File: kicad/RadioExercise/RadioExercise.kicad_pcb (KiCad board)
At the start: 2 copper layers, 22 parts, among them IC1 HT82V739, IC2 PIC16F1778-I_SP, IC3 SST26VF064B-104I_SM, J1 Conn_01x02_Female, SW1 SW_MEC_5E, SW2 SW_MEC_5E, SW3 SW_MEC_5E, SW4 SW_MEC_5E, SW5 SW_DPDT_x2

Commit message: update
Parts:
- removed D1: LED, LED_THT:LED_D5.0mm_Clear
- removed R1: 10k, Resistor_THT:R_Axial_DIN0207_L6.3mm_D2.5mm_P7.62mm_Horizontal
- removed R6: 1k, Resistor_THT:R_Axial_DIN0207_L6.3mm_D2.5mm_P7.62mm_Horizontal
- removed SW3, SW4: SW_MEC_5E, Button_Switch_THT:SW_PUSH_6mm
- SW1, SW2: value SW_MEC_5E -> SW_Push
- moved SW5 58.7 mm to (171.1, 83.6)
- moved SW1 45.2 mm to (169.4, 75.9)
- moved R3 44.1 mm to (180.0, 63.8)
- moved R5 44.1 mm to (180.0, 67.8)
- moved C3 43.2 mm to (185.9, 72.6)
- moved C1 36.0 mm to (191.2, 65.0)
- moved J1 33.9 mm to (172.9, 71.8)
- moved LS1 33.8 mm to (162.1, 75.8)
- moved IC1 32.7 mm to (158.4, 63.8)
- moved IC2 32.7 mm to (151.2, 80.3)
- moved C5 24.2 mm to (180.0, 78.2)
- moved R2 22.3 mm to (169.2, 63.8)
- moved R4 22.3 mm to (169.2, 67.8)
- moved C4 13.7 mm to (158.8, 96.5)
- moved IC3 13.5 mm to (162.0, 89.8)
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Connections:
- IC2 pad 11: Net-(IC2-Pad11) -> GND
- SW1 pad 2: Net-(SW1-Pad2) -> Net-(IC2-Pad12)
- SW2 pad 2: Net-(SW2-Pad2) -> Net-(IC2-Pad13)

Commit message: update1
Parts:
- moved R2 62.1 mm to (147.3, 121.9), turned to 90 degrees
- moved C1 59.6 mm to (147.3, 105.4), turned to 270 degrees
- moved R3 48.2 mm to (184.2, 111.8), turned to 90 degrees
- moved SW2 47.3 mm to (180.3, 121.9), turned to 180 degrees
- moved C2 46.0 mm to (156.2, 111.8), turned to 180 degrees
- moved SW1 44.4 mm to (152.4, 116.8)
- moved C3 40.6 mm to (175.3, 111.8)
- moved SW5 39.5 mm to (188.0, 119.4), turned to 90 degrees
- moved R5 35.7 mm to (151.1, 88.9)
- moved R4 33.1 mm to (147.3, 92.7), turned to 270 degrees
- moved IC1 29.8 mm to (151.1, 92.7)
- moved IC2 29.4 mm to (166.4, 105.4)
- moved J1 27.2 mm to (186.7, 95.2), turned to 270 degrees
- moved LS1 26.0 mm to (143.5, 94.0), turned to 270 degrees
- moved IC3 18.0 mm to (176.5, 100.3), turned to 90 degrees
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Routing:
- net VDD: track 0.00 -> 110.4 mm
- net Net-(J1-Pad2): track 0.00 -> 18.3 mm

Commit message: remove wire
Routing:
- net VDD: track 110.4 -> 0.00 mm
- net Net-(J1-Pad2): track 18.3 -> 0.00 mm

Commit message: wire
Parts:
- J1, LS1: moved to B.Cu
- moved C3 47.8 mm to (207.0, 76.0), turned to 270 degrees
- moved J1 46.7 mm to (215.9, 58.8), turned to 90 degrees
- moved LS1 46.4 mm to (174.0, 59.0), turned to 90 degrees
- moved R5 46.4 mm to (181.7, 53.9)
- moved SW1 46.4 mm to (182.9, 81.9)
- moved C1 46.4 mm to (177.8, 70.4)
- moved C4 46.4 mm to (184.2, 70.4)
- moved IC1 46.4 mm to (181.7, 57.7)
- moved IC2 46.4 mm to (196.9, 70.4)
- moved R2 46.4 mm to (177.8, 86.9)
- moved R4 46.4 mm to (177.8, 57.7)
- moved SW2 46.4 mm to (210.9, 86.9)
- moved C2 45.7 mm to (187.0, 78.0), turned to 90 degrees
- moved R3 45.0 mm to (212.4, 76.8)
- moved SW5 44.4 mm to (216.0, 84.9)
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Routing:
- net VDD: track 0.00 -> 103.1 mm
- net GND: track 0.00 -> 87.5 mm, vias 0 -> 1
- net Net-(IC1-Pad5): track 0.00 -> 44.2 mm
- net Net-(J1-Pad2): track 0.00 -> 28.4 mm, vias 0 -> 1
- net Net-(IC2-Pad13): track 0.00 -> 25.3 mm
- net Net-(IC2-Pad3): track 0.00 -> 20.7 mm
- net Net-(IC1-Pad7): track 0.00 -> 18.6 mm, vias 0 -> 1
- net Net-(IC2-Pad12): track 0.00 -> 17.8 mm
- net Net-(C1-Pad2): track 0.00 -> 16.7 mm
- net Net-(IC1-Pad1): track 0.00 -> 14.0 mm, vias 0 -> 1
- net Net-(IC2-Pad25): track 0.00 -> 11.3 mm, vias 0 -> 1
- net Net-(IC2-Pad24): track 0.00 -> 10.9 mm
- net Net-(IC2-Pad23): track 0.00 -> 10.5 mm, vias 0 -> 1
- net Net-(C4-Pad1): track 0.00 -> 8.67 mm
- net Net-(IC2-Pad22): track 0.00 -> 5.68 mm
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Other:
- board outline added: 50 x 40 mm
- board text added: "GND"
- board text added: "NEG"
- board text added: "POS"
- board text added: "VCC"

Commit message: update
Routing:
- added copper zone on B.Cu, net GND
- added copper zone on F.Cu, net VDD

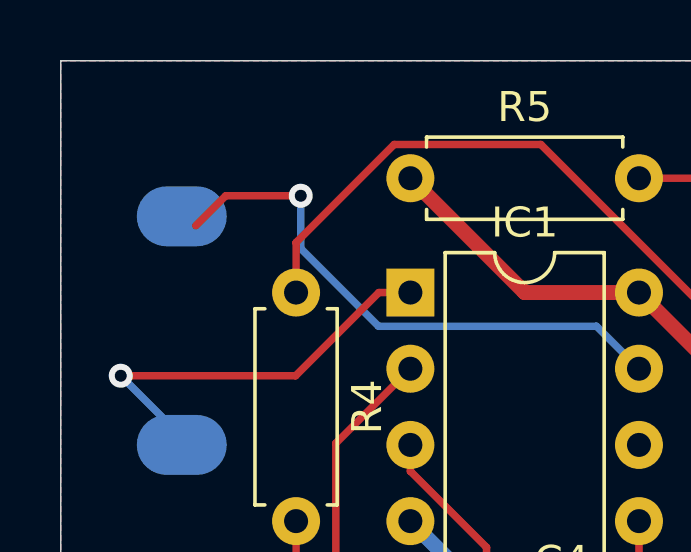
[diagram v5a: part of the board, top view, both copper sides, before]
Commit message: 配線が繋がってなかったので修正
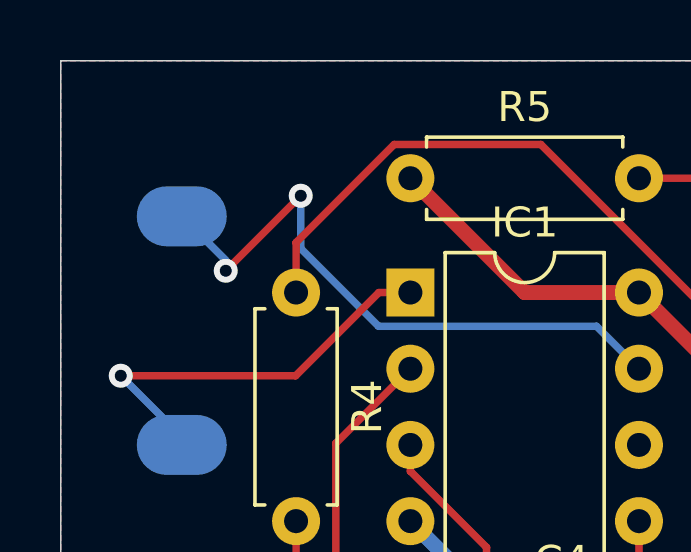
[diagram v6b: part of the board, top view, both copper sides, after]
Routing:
- net Net-(IC1-Pad7): track 18.6 -> 20.6 mm, vias 1 -> 2
